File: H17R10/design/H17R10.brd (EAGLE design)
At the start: 60 x 60.6 mm, 72 parts, among them J1 3-644456-2, P1 HEXABIT_17.32_X3_NO_P1_P2_P3_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, U1 STM32G0B1CEU6NUFQFPN48_STM32_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, U2 POWERSTEP01, X1 8MHZ

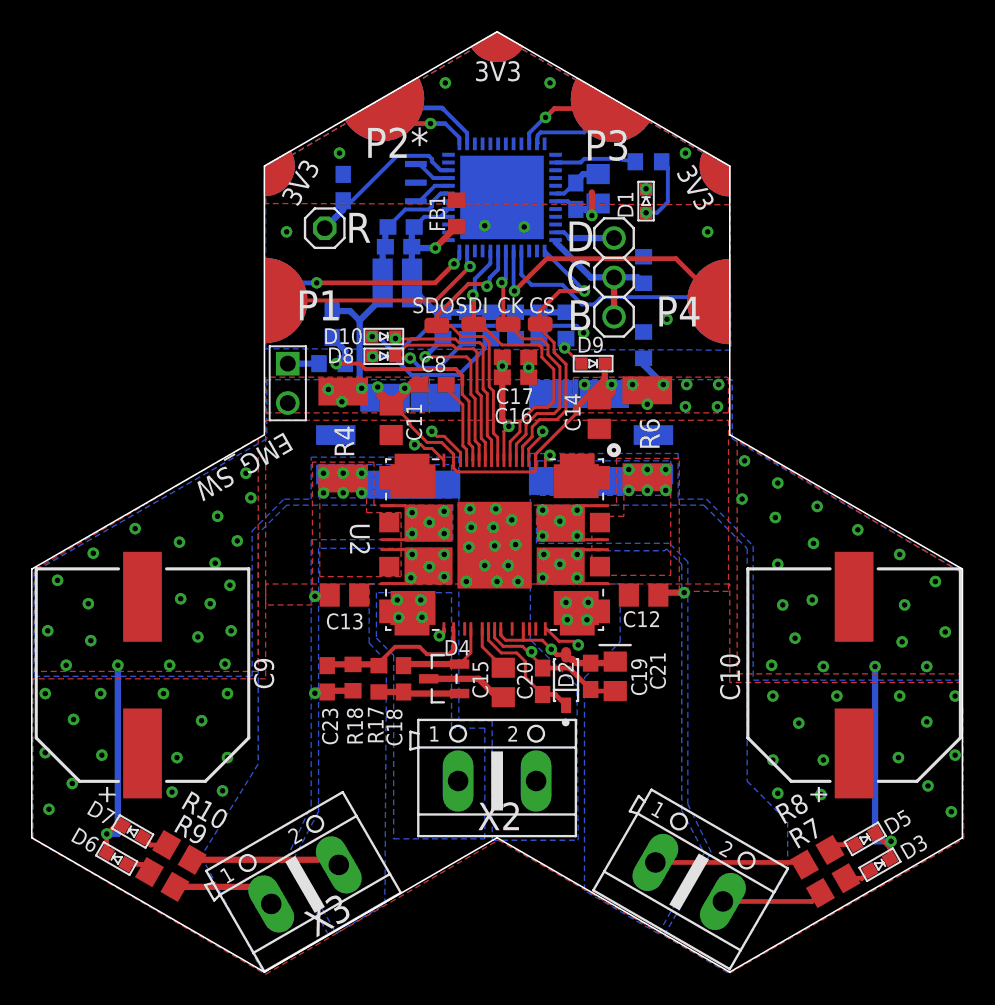
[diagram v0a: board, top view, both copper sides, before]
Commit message: -Connect missing wires - Delete power led - Improve the layout for better performance and appearance
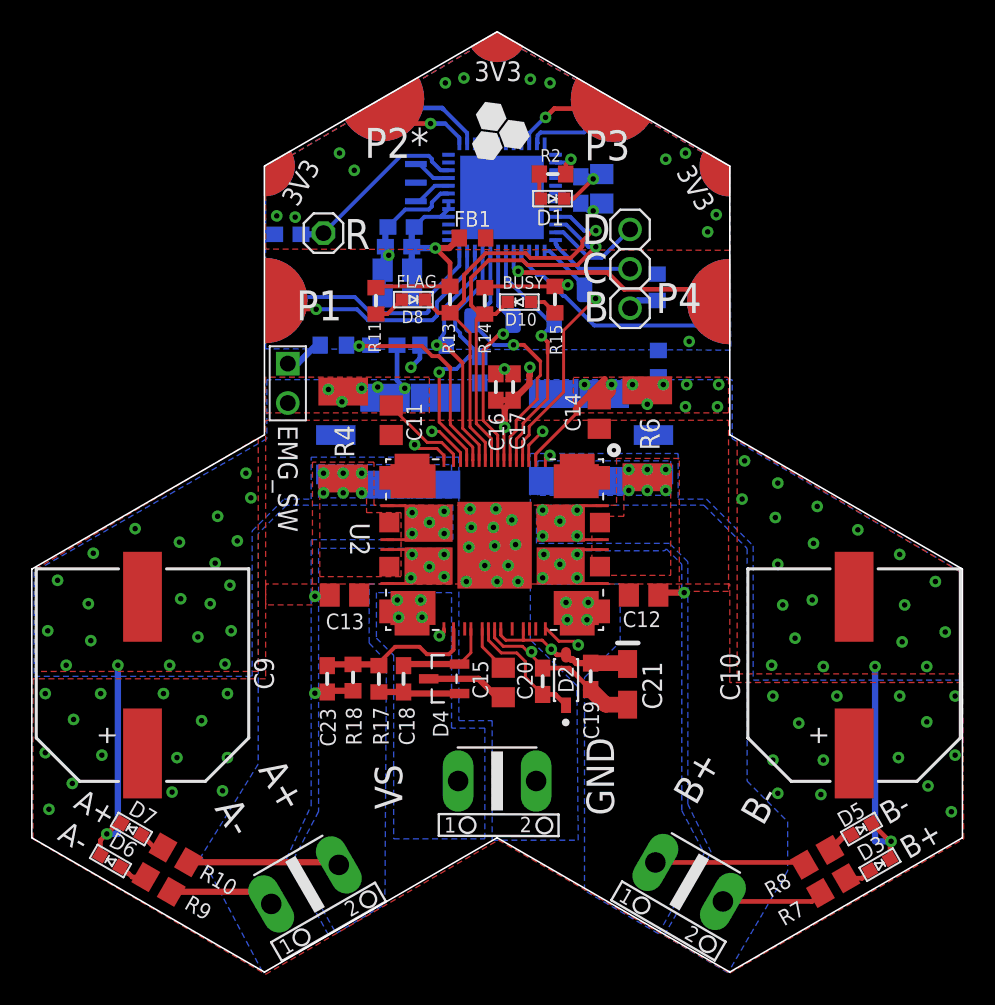
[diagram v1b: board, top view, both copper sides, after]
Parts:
- removed D9: Green, HEXABITZ_USER_INTERFACE_PARTS:VLMTG1300-GS08
- removed JP1: (no value), HEXABITZ_USER_INTERFACE_PARTS:1X01
- removed JP2: (no value), pinhead:1X03
- removed R12: 330, HEXABITZ_RCLS:R-0603
- added R: (no value), HEXABITZ_USER_INTERFACE_PARTS:1X01
- added SWD: (no value), pinhead:1X03
- C21: device HEXABITZ_RCLS:C-0805-POL -> HEXABITZ_RCLS:T491A
- U1: device HEXABITZ_ICs:UFQFPN48_STM32_STM -> HEXABITZ_ICs:HEXABITZ_ICS_UFQFPN48_STM32_STM
- moved D10 9.01 mm to (1.43, 34.5), turned to 270 degrees
- moved R11 7.58 mm to (-7.81, 34.6), flipped to the top
- moved R2 6.24 mm to (3.57, 42.8), flipped to the top
- moved D1 6.03 mm to (3.57, 41.2), turned to 90 degrees
- moved SDO 4.93 mm to (1.03, 33.3), flipped to the bottom, turned to 90 degrees
- moved C1 4.68 mm to (-13.5, 38.9), turned to 180 degrees
- moved D8 4.12 mm to (-5.40, 34.7)
- moved R14 3.84 mm to (-0.79, 34.6), flipped to the top
- moved CS 3.62 mm to (5.64, 35.3), flipped to the bottom, turned to 90 degrees
- moved C22 3.60 mm to (-7.30, 31.8), turned to 180 degrees
- moved C8 3.16 mm to (-1.11, 30.2), flipped to the bottom, turned to 270 degrees
- moved R15 3.04 mm to (3.73, 34.7), flipped to the top
- moved CK 2.97 mm to (3.68, 33.3), flipped to the bottom, turned to 90 degrees
- moved R13 2.01 mm to (-3.03, 34.7), flipped to the top
- moved C17 1.91 mm to (1.03, 29.1), turned to 270 degrees
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- renumbered J1 to EMG_SW, P1 to U$1, SJ1 to SA_J, SJ2 to SB_J, X2 to PWR, X3 to A, X4 to B
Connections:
- removed net N$14: D9.A, R12.1
- net BUSY/SYNC: now also U1.34
- net C: now also SWD.1, SWD.2; no longer JP2.1, JP2.2
- net D: now also SWD.3; no longer JP2.3
- net FLAG: now also U1.33
- net N$12: now also R.1; no longer JP1.1
- net RESET: now also U1.45
- net STCK: now also U1.46
- net VDDA: no longer R12.2
- net VSSA: no longer D9.C
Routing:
- net VDDA: track 66.4 -> 86.6 mm, vias 4 -> 6
- net RESET: track 5.43 -> 17.6 mm, vias 0 -> 1
- net FLAG: track 18.7 -> 28.4 mm
- net N$5: track 10.7 -> 1.84 mm, vias 1 -> 0
- net N$13: track 9.27 -> 2.05 mm, vias 1 -> 0
- net STCK: track 11.3 -> 17.1 mm
- net VSSA: track 116.8 -> 112.7 mm, vias 75 -> 76
- net SDO: track 19.0 -> 15.2 mm
- net N$17: track 5.25 -> 2.16 mm, vias 0 -> 1
- net N$19: track 4.46 -> 1.63 mm, vias 1 -> 0
- net USART5_TX: track 17.8 -> 15.3 mm
- net N$14: track 2.42 -> 0.00 mm, vias 1 -> 0
- net D: track 3.92 -> 6.24 mm
- net N$3: track 16.8 -> 14.7 mm
- net CS: track 19.2 -> 17.1 mm
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- added copper zone on layer 2, net VDD
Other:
- board text added: "85V MAX"
- board text added: "A+"
- board text added: "A-"
- board text added: "B+"
- board text added: "B-"
- board text added: "BUSY"
- board text added: "FLAG"
- board text added: "H17R10"
- board text added: "VS"
